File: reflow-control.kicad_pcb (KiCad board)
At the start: 2 copper layers, 56.6 x 115.8 mm, 27 parts, among them P1 CONN_2, P10 CONN_01X01, P11 CONN_01X01, P12 CONN_02X07, P15 CONN_01X07, P16 CONN_01X01, P17 CONN_01X01, P2 SPI_ADC, P4 ANALOG_IN, P7 TRIAC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

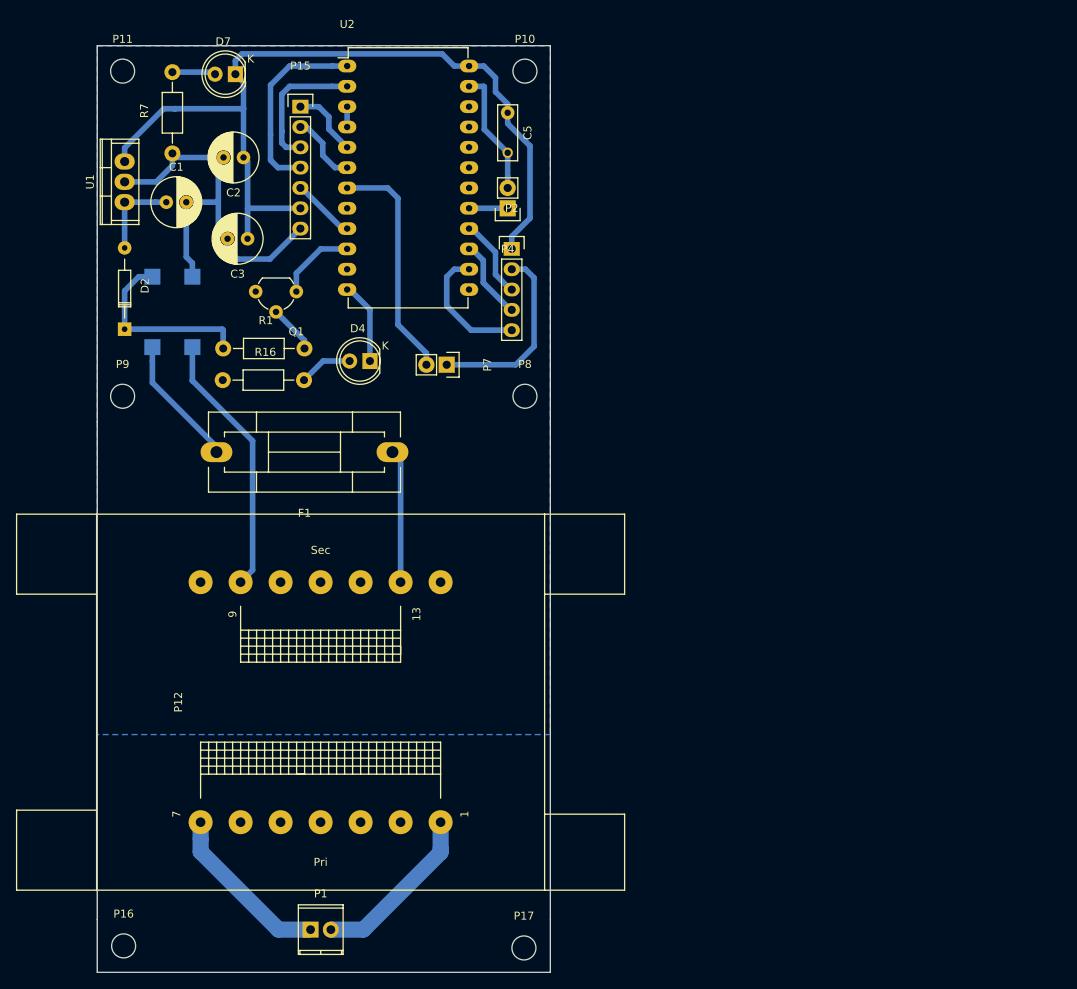
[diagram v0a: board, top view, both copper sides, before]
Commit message: rotate control pcb
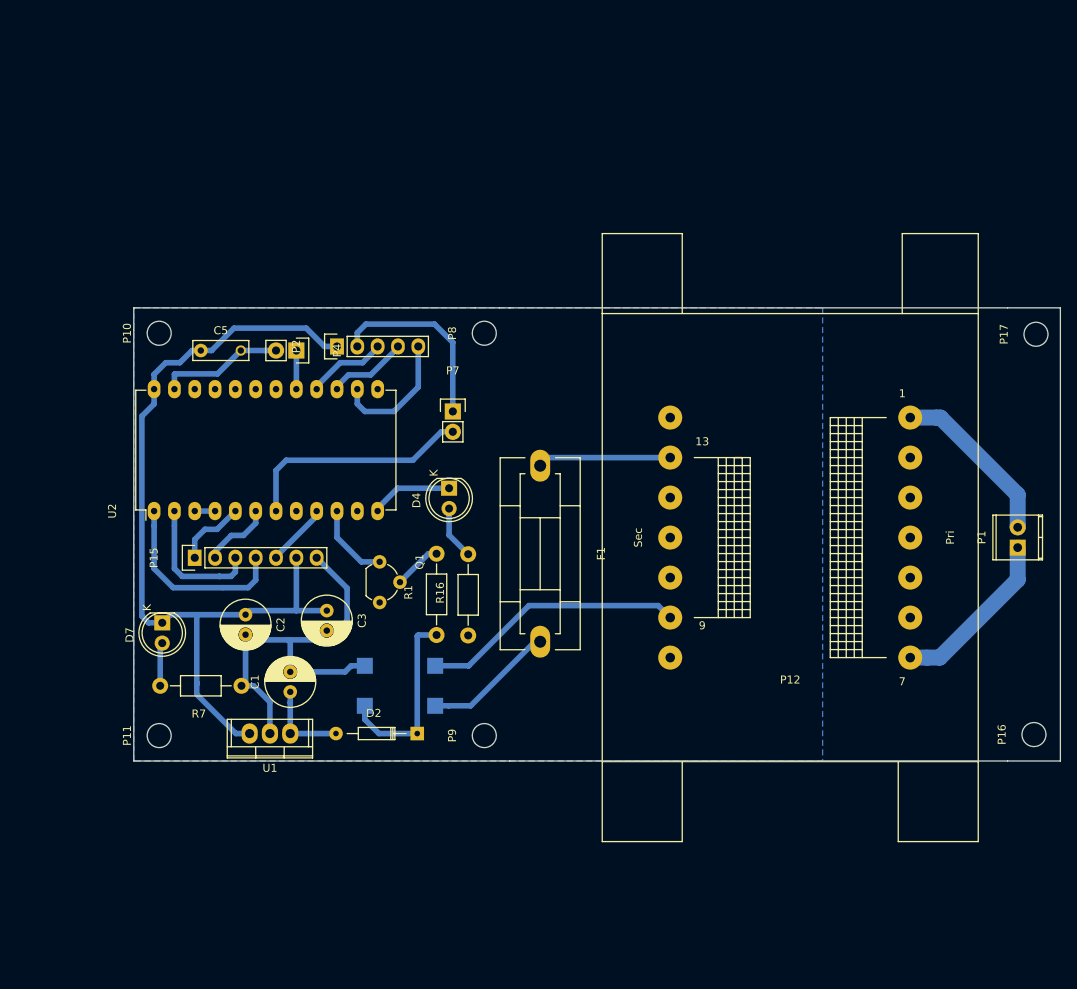
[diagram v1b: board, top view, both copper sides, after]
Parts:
- moved P16 116.8 mm to (164.8, 128.8), turned to 90 degrees
- moved P1 100.5 mm to (162.8, 105.4), turned to 90 degrees
- moved P17 99.9 mm to (165.1, 78.7), turned to 90 degrees
- moved P11 83.2 mm to (55.5, 128.9), turned to 90 degrees
- moved R7 71.7 mm to (60.7, 122.7), turned to 180 degrees
- moved U1 71.3 mm to (69.3, 128.7), turned to 180 degrees
- moved D7 69.2 mm to (55.9, 114.8), turned to 270 degrees
- moved C1 63.1 mm to (71.9, 123.4), turned to 90 degrees
- moved D2 62.4 mm to (87.8, 128.6), turned to 180 degrees
- moved P12 62.2 mm to (134.4, 104.2), turned to 180 degrees
- moved P9 62.0 mm to (96.1, 128.9), turned to 90 degrees
- moved U2 60.6 mm to (54.9, 100.8), turned to 90 degrees
- moved P15 57.9 mm to (59.9, 106.7), turned to 90 degrees
- moved C2 57.2 mm to (66.3, 113.8), turned to 270 degrees
- moved P10 56.2 mm to (55.5, 78.6), turned to 90 degrees
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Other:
- board size 56.6 x 115.8 mm -> 115.8 x 56.6 mm
